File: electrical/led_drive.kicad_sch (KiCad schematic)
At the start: 14 parts, among them J1 Screw_Terminal_01x01, J2 Screw_Terminal_01x01, J3 Ground connector from bulb wi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, Q1 IRF5305, Q2 BC547

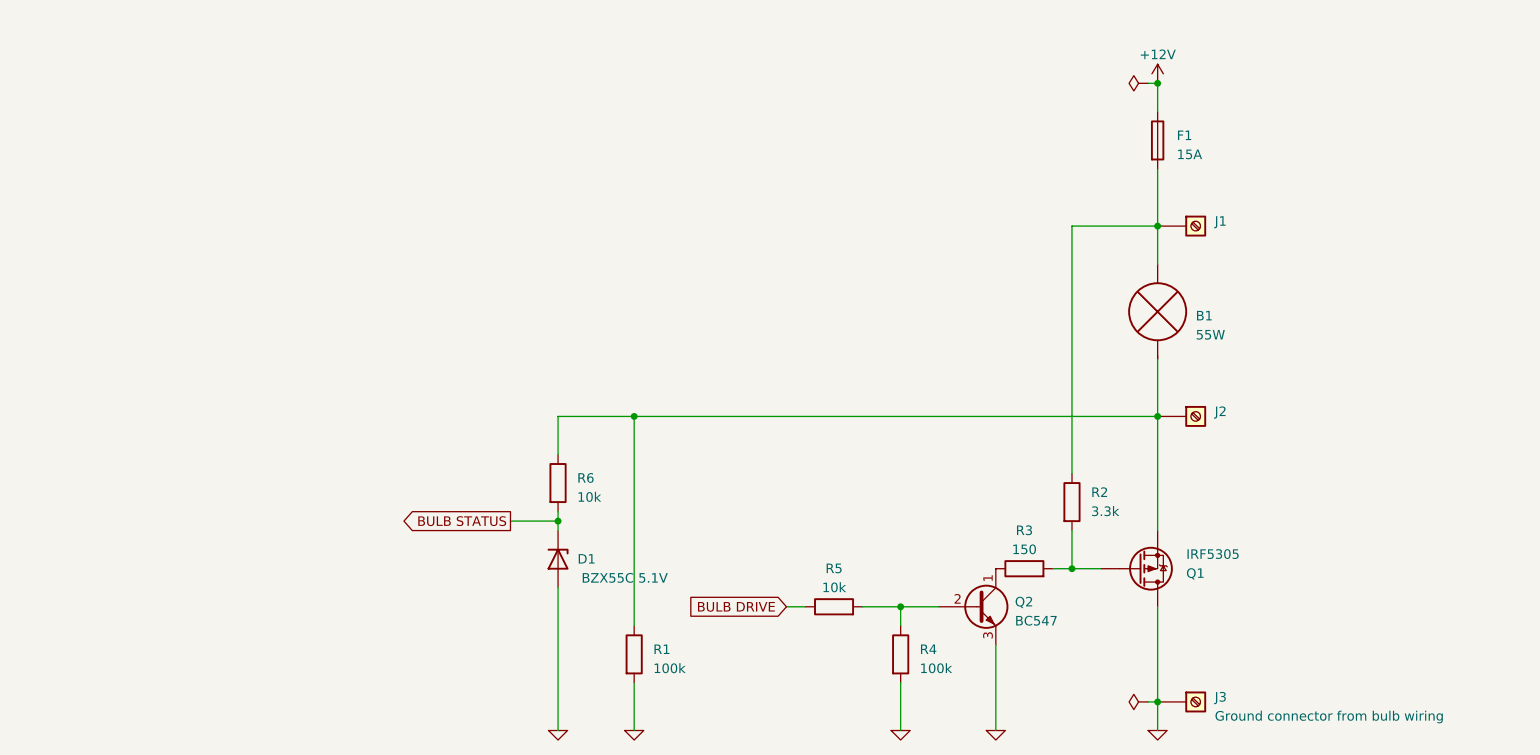
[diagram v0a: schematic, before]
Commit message: Added electrical diagram
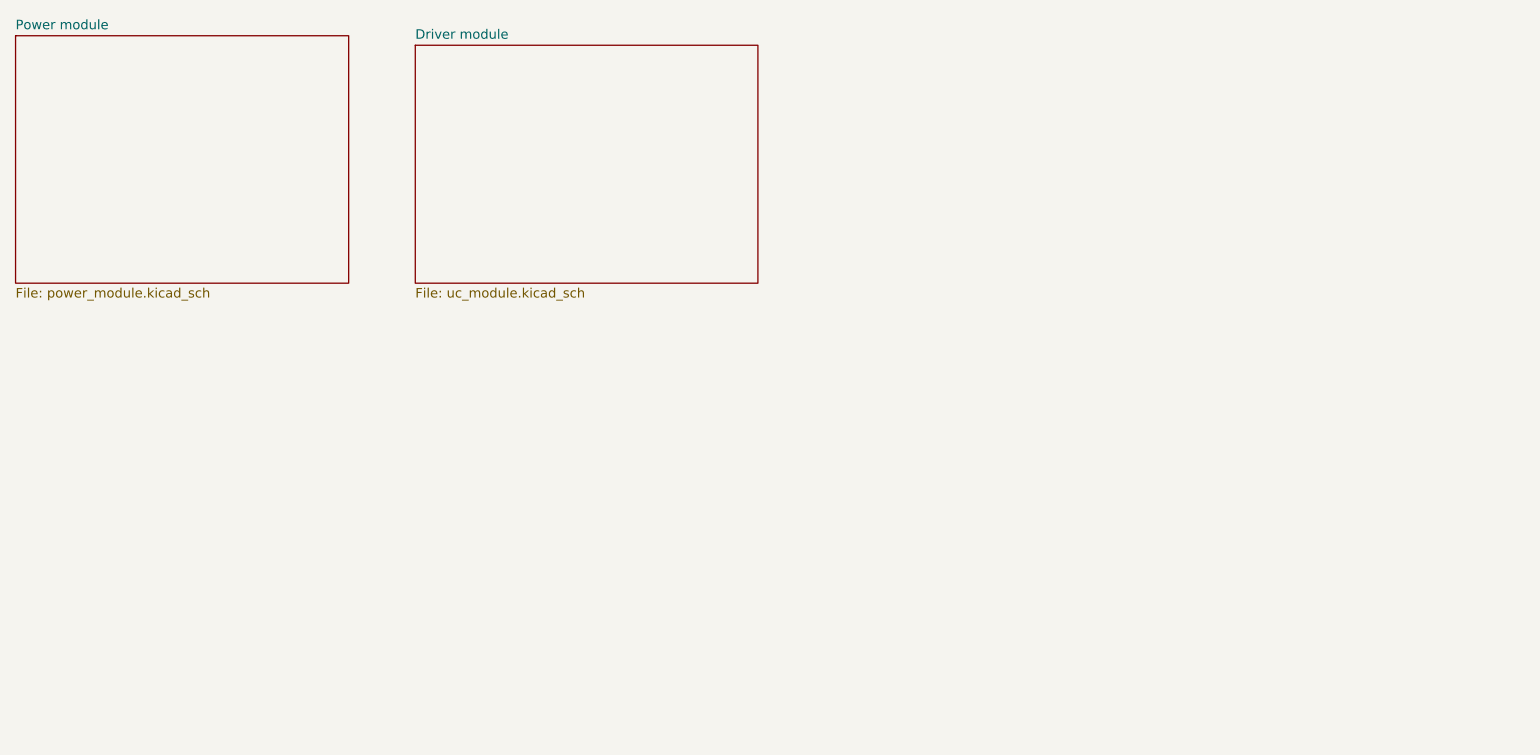
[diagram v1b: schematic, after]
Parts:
- removed B1: 55W, symbol bulb:Bulb
- removed D1: BZX55C 5.1V, Package_TO_SOT_SMD:SOT-23, symbol Diode:BZX84Cxx
- removed F1: 15A, symbol Device:Fuse
- removed J1, J2: Screw_Terminal_01x01, symbol Connector:Screw_Terminal_01x01
- removed J3: Ground connector from bulb wiring, symbol Connector:Screw_Terminal_01x01
- removed Q1: IRF5305, Package_TO_SOT_THT:TO-220-3_Vertical, symbol Transistor_FET:IRF4905
- removed Q2: BC547, Package_TO_SOT_THT:TO-92_Inline, symbol Transistor_BJT:BC547
- removed R1, R4: 100k, symbol Device:R
- removed R2: 3.3k, symbol Device:R
- removed R3: 150, symbol Device:R
- removed R5, R6: 10k, symbol Device:R
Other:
- added sheet Driver module (uc_module.kicad_sch)
- added sheet Power module (power_module.kicad_sch)
- title: Power module -> Bulb drive

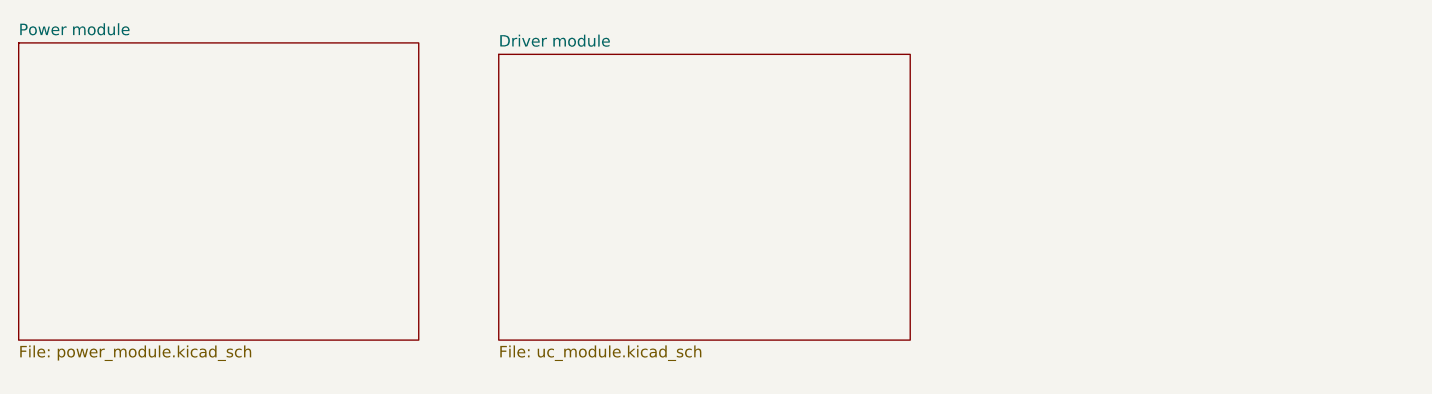
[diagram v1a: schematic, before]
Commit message: Added power module with MOSFET-N
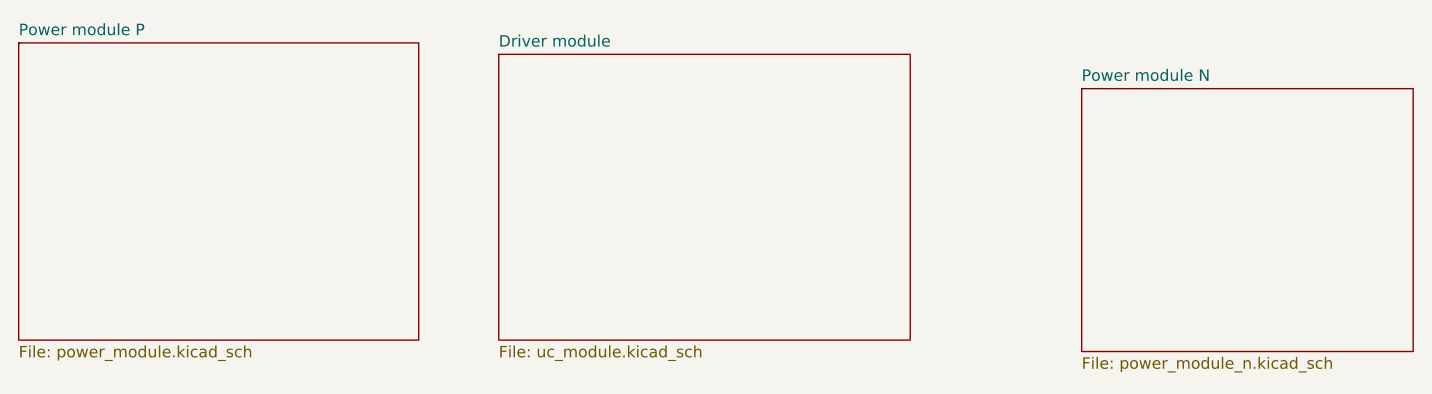
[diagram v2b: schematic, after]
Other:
- sheet Power module renamed Power module P
- added sheet Power module N (power_module_n.kicad_sch)
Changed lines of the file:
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@@
+    )
+  )
+  (sheet (at 144.78 39.37) (size 36.83 29.21) (fields_autoplaced)
+    (stroke (width 0.1524) (type solid))
+    (fill (color 0 0 0 0.0000))
+    (property "Sheetname" "Power module N" (at 144.78 38.6584 0)
+      (effects (font (size 1.27 1.27)) (justify left bottom))
+    )
+    (property "Sheetfile" "power_module_n.kicad_sch" (at 144.78 69.1646 0)
+      (effects (font (size 1.27 1.27)) (justify left top))
+    )
+    (instances
+      (project "led_drive"
+        (path "/01e69042-7c7e-48e9-b7c3-459316fd17f1" (page "4"))
+      )
     )
   )
@@
     (stroke (width 0.1524) (type solid))
     (fill (color 0 0 0 0.0000))
-    (property "Sheetname" "Power module" (at 26.67 33.5784 0)
+    (property "Sheetname" "Power module P" (at 26.67 33.5784 0)
       (effects (font (size 1.27 1.27)) (justify left bottom))
     )
